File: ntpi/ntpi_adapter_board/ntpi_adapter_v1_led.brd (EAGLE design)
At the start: 35.9 x 14.1 mm, 7 parts, among them Q1 BC849C

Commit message: NTPi adapter board v1.1
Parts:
- turned R2 to 270 degrees
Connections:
- removed net N$9: LED1.A, R2.2
- new net N$2: LED1.A, R2.1
- net +5V: now also R2.2; no longer R2.1
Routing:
- net N$9: track 3.67 -> 0.00 mm
- net N$2: track 0.00 -> 3.67 mm
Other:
- board text added: "v1.1 2013-03"
- board text removed: "3V3"
- board text removed: "v1.0 2013-02"

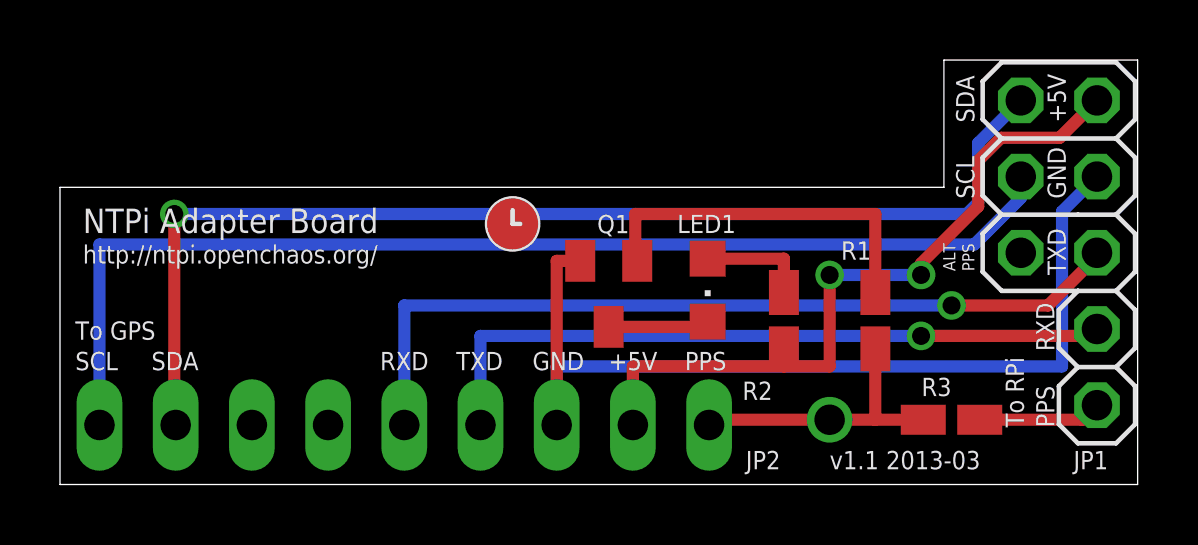
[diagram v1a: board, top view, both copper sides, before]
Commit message: silk screen font changes
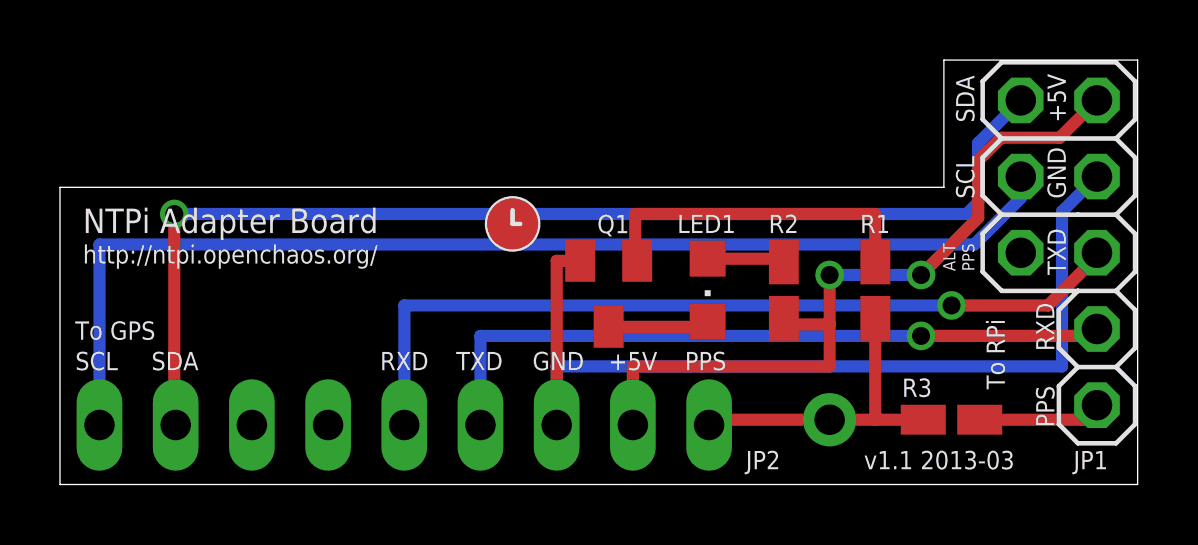
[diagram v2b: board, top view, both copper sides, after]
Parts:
- moved R1 1.02 mm to (27.2, 6.48)
- moved R2 1.02 mm to (24.1, 6.48)
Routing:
- net PPS: track 9.58 -> 10.6 mm
- net N$4: track 12.2 -> 11.2 mm
- net N$2: track 3.67 -> 2.65 mm
- net +5V: track 24.8 -> 25.7 mm
